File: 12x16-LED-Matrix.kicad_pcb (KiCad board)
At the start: 2 copper layers, 56 x 45 mm, 197 parts, among them J1 Conn_01x16, J2 Conn_01x12

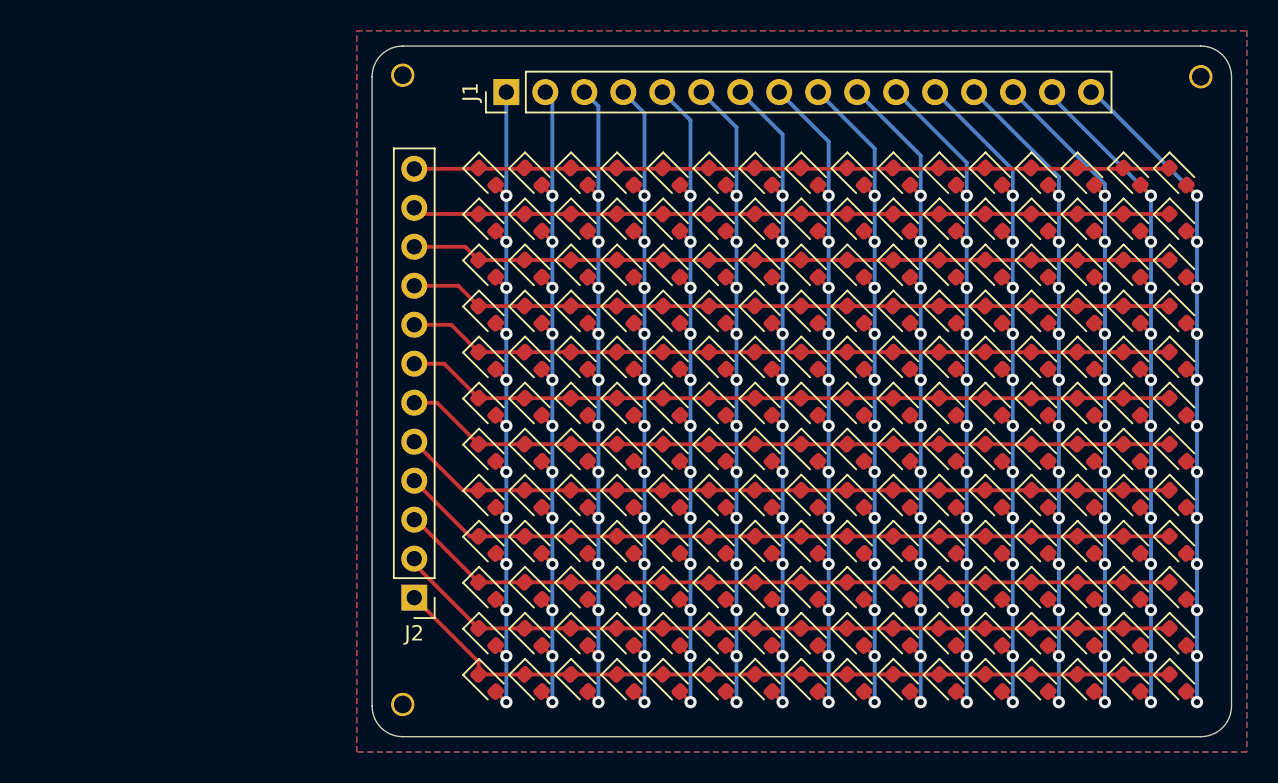
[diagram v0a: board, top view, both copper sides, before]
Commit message: Add silkscreen
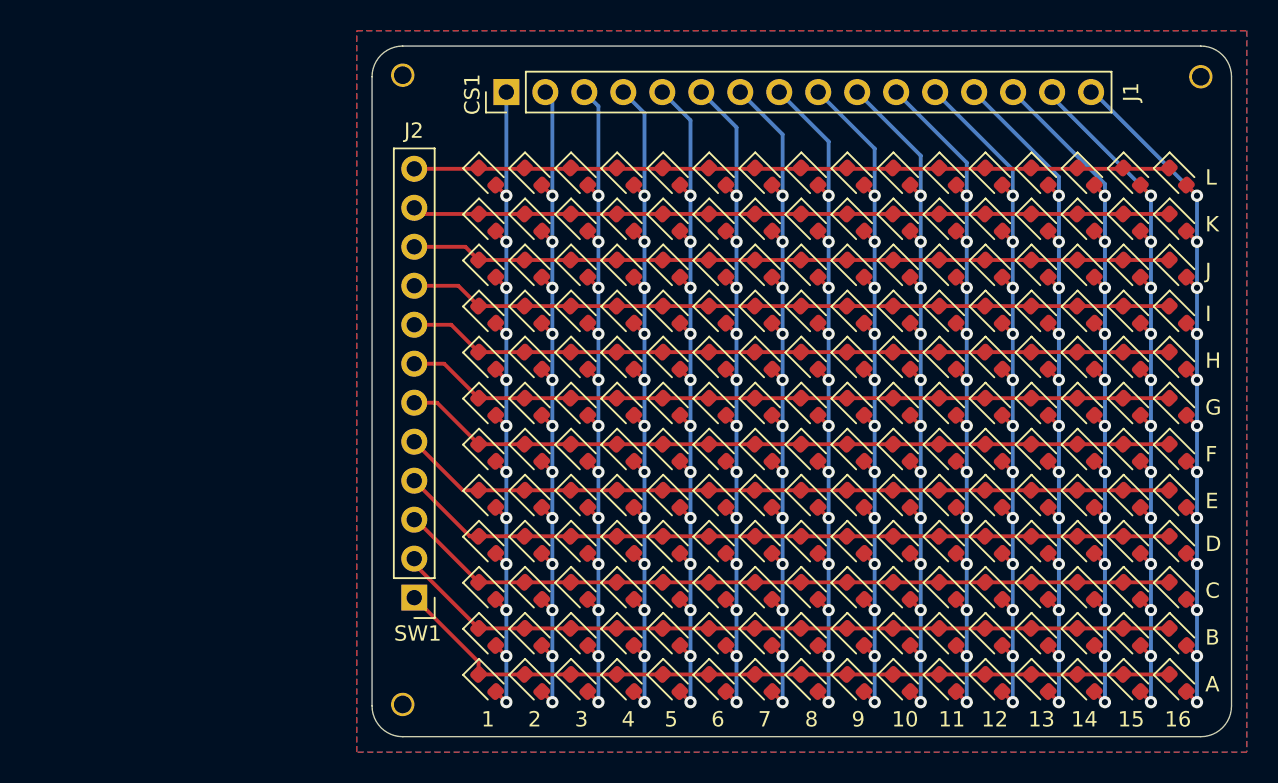
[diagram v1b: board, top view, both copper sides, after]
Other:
- board text added: "1"
- board text added: "10"
- board text added: "11"
- board text added: "12"
- board text added: "13"
- board text added: "14"
- board text added: "15"
- board text added: "16"
- board text added: "2"
- board text added: "3"
- board text added: "4"
- board text added: "5"
- board text added: "6"
- board text added: "7"
- board text added: "8"
- board text added: "9"
- board text added: "A"
- board text added: "B"
- board text added: "C"
- board text added: "CS1"
- board text added: "CS10"
- board text added: "CS11"
- board text added: "CS12"
- board text added: "CS13"
- board text added: "CS14"
- board text added: "CS15"
- board text added: "CS16"
- board text added: "CS2"
- board text added: "CS3"
- board text added: "CS4"
- board text added: "CS5"
- board text added: "CS6"
- board text added: "CS7"
- board text added: "CS8"
- board text added: "CS9"
- board text added: "D"
- board text added: "E"
- board text added: "F"
- board text added: "G"
- board text added: "H"
- board text added: "I"
- board text added: "J"
- board text added: "K"
- board text added: "L"
- board text added: "SW1"
- board text added: "SW10"
- board text added: "SW11"
- board text added: "SW12"
- board text added: "SW2"
- board text added: "SW3"
- board text added: "SW4"
- board text added: "SW5"
- board text added: "SW6"
- board text added: "SW7"
- board text added: "SW8"
- board text added: "SW9"

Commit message: Add ground pins, fix silkscreen
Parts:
- J1: value Conn_01x16 -> Conn_01x17; footprint Connector_PinHeader_2.54mm:PinHeader_1x16_P2.54mm_Vertical -> Connector_PinHeader_2.54mm:PinHeader_1x17_P2.54mm_Vertical
- J2: value Conn_01x12 -> Conn_01x13; footprint Connector_PinHeader_2.54mm:PinHeader_1x12_P2.54mm_Vertical -> Connector_PinHeader_2.54mm:PinHeader_1x13_P2.54mm_Vertical
- moved J1 0.50 mm to (83.8, 62.5)
- moved J2 0.26 mm to (78.0, 95.0)
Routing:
- added copper zone on B.Cu, net GND
- added copper zone on F.Cu, net GND
- removed copper zone on B.Cu, net (none)
- removed copper zone on F.Cu, net (none)
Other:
- board text added: "%%version%% %%date%%"
- board text added: "GND"
- board text added: "JLCJLCJLCJLC"
- board text removed: "16x12 LED matrix %%version%% %%date%%"

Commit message: Add driver directly to schematic
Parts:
- removed J2: Conn_01x13, Connector_PinHeader_2.54mm:PinHeader_1x13_P2.54mm_Vertical
- added C1: 0.47uF, Capacitor_SMD:C_0402_1005Metric, F.Cu at (57.9, 74.8)
- added C2: 0.47uF, Capacitor_SMD:C_0402_1005Metric, F.Cu at (60.8, 74.8)
- added C3: 0.47uF, Capacitor_SMD:C_0402_1005Metric, F.Cu at (57.9, 76.7)
- added C4: 0.1uF, Capacitor_SMD:C_0402_1005Metric, F.Cu at (57.9, 78.7)
- added C5: 0.1uF, Capacitor_SMD:C_0402_1005Metric, F.Cu at (69.1, 68.5)
- added C6: 0.1uF, Capacitor_SMD:C_0402_1005Metric, F.Cu at (60.8, 76.7)
- added C7: 0.47uF, Capacitor_SMD:C_0402_1005Metric, F.Cu at (72.0, 66.5)
- added R1: 100k, Resistor_SMD:R_0402_1005Metric, F.Cu at (66.2, 66.5)
- added R2: 100k, Resistor_SMD:R_0402_1005Metric, F.Cu at (69.1, 66.5)
- added R3: 100k, Resistor_SMD:R_0402_1005Metric, F.Cu at (66.2, 68.5)
- added R4: 20k, Resistor_SMD:R_0402_1005Metric, F.Cu at (66.2, 70.5)
- added U1: IS31FL3733B, Package_DFN_QFN:QFN-48-1EP_6x6mm_P0.4mm_EP4.3x4.3mm_ThermalVias, F.Cu at (60.6, 69.7)
- J1: value Conn_01x17 -> Conn_01x06; footprint Connector_PinHeader_2.54mm:PinHeader_1x17_P2.54mm_Vertical -> Connector_PinHeader_2.54mm:PinHeader_1x06_P2.54mm_Vertical
- moved J1 30.1 mm to (54.1, 67.9), turned to 0 degrees
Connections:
- net Net-(D1-Pad1) renamed SW1
- net Net-(D100-Pad1) renamed SW7
- net Net-(D113-Pad1) renamed SW8
- net Net-(D129-Pad1) renamed SW9
- net Net-(D145-Pad1) renamed SW10
- net Net-(D161-Pad1) renamed SW11
- net Net-(D17-Pad1) renamed SW2
- net Net-(D177-Pad1) renamed SW12
- net Net-(D33-Pad1) renamed SW3
- net Net-(D49-Pad1) renamed SW4
- net Net-(D65-Pad1) renamed SW5
- net Net-(D81-Pad1) renamed SW6
- D1 pad 2: Net-(D1-Pad2) -> CS1
- D10 pad 2: Net-(D10-Pad2) -> CS10
- D100 pad 2: Net-(D100-Pad2) -> CS4
- D101 pad 2: Net-(D101-Pad2) -> CS5
- D102 pad 2: Net-(D102-Pad2) -> CS6
- D103 pad 2: Net-(D103-Pad2) -> CS7
- D104 pad 2: Net-(D104-Pad2) -> CS8
- D105 pad 2: Net-(D105-Pad2) -> CS9
- D106 pad 2: Net-(D10-Pad2) -> CS10
- D107 pad 2: Net-(D107-Pad2) -> CS11
- D108 pad 2: Net-(D108-Pad2) -> CS12
- D109 pad 2: Net-(D109-Pad2) -> CS13
- D11 pad 2: Net-(D107-Pad2) -> CS11
- D110 pad 2: Net-(D110-Pad2) -> CS14
- D111 pad 2: Net-(D111-Pad2) -> CS15
- D112 pad 2: Net-(D112-Pad2) -> CS16
- D113 pad 2: Net-(D1-Pad2) -> CS1
- D114 pad 2: Net-(D114-Pad2) -> CS2
- D115 pad 2: Net-(D115-Pad2) -> CS3
- D116 pad 2: Net-(D100-Pad2) -> CS4
- D117 pad 2: Net-(D101-Pad2) -> CS5
- D118 pad 2: Net-(D102-Pad2) -> CS6
- D119 pad 2: Net-(D103-Pad2) -> CS7
- D12 pad 2: Net-(D108-Pad2) -> CS12
- D120 pad 2: Net-(D104-Pad2) -> CS8
- D121 pad 2: Net-(D105-Pad2) -> CS9
- D122 pad 2: Net-(D10-Pad2) -> CS10
- D123 pad 2: Net-(D107-Pad2) -> CS11
- D124 pad 2: Net-(D108-Pad2) -> CS12
- D125 pad 2: Net-(D109-Pad2) -> CS13
- D126 pad 2: Net-(D110-Pad2) -> CS14
- D127 pad 2: Net-(D111-Pad2) -> CS15
- D128 pad 2: Net-(D112-Pad2) -> CS16
- D129 pad 2: Net-(D1-Pad2) -> CS1
- D13 pad 2: Net-(D109-Pad2) -> CS13
- D130 pad 2: Net-(D114-Pad2) -> CS2
- D131 pad 2: Net-(D115-Pad2) -> CS3
- D132 pad 2: Net-(D100-Pad2) -> CS4
- D133 pad 2: Net-(D101-Pad2) -> CS5
- D134 pad 2: Net-(D102-Pad2) -> CS6
- D135 pad 2: Net-(D103-Pad2) -> CS7
- D136 pad 2: Net-(D104-Pad2) -> CS8
- D137 pad 2: Net-(D105-Pad2) -> CS9
- D138 pad 2: Net-(D10-Pad2) -> CS10
- D139 pad 2: Net-(D107-Pad2) -> CS11
- D14 pad 2: Net-(D110-Pad2) -> CS14
- D140 pad 2: Net-(D108-Pad2) -> CS12
- D141 pad 2: Net-(D109-Pad2) -> CS13
- D142 pad 2: Net-(D110-Pad2) -> CS14
- D143 pad 2: Net-(D111-Pad2) -> CS15
- D144 pad 2: Net-(D112-Pad2) -> CS16
- D145 pad 2: Net-(D1-Pad2) -> CS1
- D146 pad 2: Net-(D114-Pad2) -> CS2
- D147 pad 2: Net-(D115-Pad2) -> CS3
- D148 pad 2: Net-(D100-Pad2) -> CS4
- D149 pad 2: Net-(D101-Pad2) -> CS5
- D15 pad 2: Net-(D111-Pad2) -> CS15
- D150 pad 2: Net-(D102-Pad2) -> CS6
- D151 pad 2: Net-(D103-Pad2) -> CS7
- D152 pad 2: Net-(D104-Pad2) -> CS8
- D153 pad 2: Net-(D105-Pad2) -> CS9
- D154 pad 2: Net-(D10-Pad2) -> CS10
- D155 pad 2: Net-(D107-Pad2) -> CS11
- D156 pad 2: Net-(D108-Pad2) -> CS12
- D157 pad 2: Net-(D109-Pad2) -> CS13
- D158 pad 2: Net-(D110-Pad2) -> CS14
- D159 pad 2: Net-(D111-Pad2) -> CS15
- D16 pad 2: Net-(D112-Pad2) -> CS16
- D160 pad 2: Net-(D112-Pad2) -> CS16
- D161 pad 2: Net-(D1-Pad2) -> CS1
- D162 pad 2: Net-(D114-Pad2) -> CS2
- D163 pad 2: Net-(D115-Pad2) -> CS3
- D164 pad 2: Net-(D100-Pad2) -> CS4
- D165 pad 2: Net-(D101-Pad2) -> CS5
- D166 pad 2: Net-(D102-Pad2) -> CS6
- D167 pad 2: Net-(D103-Pad2) -> CS7
- D168 pad 2: Net-(D104-Pad2) -> CS8
- D169 pad 2: Net-(D105-Pad2) -> CS9
- D17 pad 2: Net-(D1-Pad2) -> CS1
- D170 pad 2: Net-(D10-Pad2) -> CS10
- D171 pad 2: Net-(D107-Pad2) -> CS11
- D172 pad 2: Net-(D108-Pad2) -> CS12
- D173 pad 2: Net-(D109-Pad2) -> CS13
- D174 pad 2: Net-(D110-Pad2) -> CS14
- D175 pad 2: Net-(D111-Pad2) -> CS15
- D176 pad 2: Net-(D112-Pad2) -> CS16
- D177 pad 2: Net-(D1-Pad2) -> CS1
- D178 pad 2: Net-(D114-Pad2) -> CS2
- D179 pad 2: Net-(D115-Pad2) -> CS3
- D18 pad 2: Net-(D114-Pad2) -> CS2
- D180 pad 2: Net-(D100-Pad2) -> CS4
- D181 pad 2: Net-(D101-Pad2) -> CS5
- D182 pad 2: Net-(D102-Pad2) -> CS6
- D183 pad 2: Net-(D103-Pad2) -> CS7
- D184 pad 2: Net-(D104-Pad2) -> CS8
- D185 pad 2: Net-(D105-Pad2) -> CS9
- D186 pad 2: Net-(D10-Pad2) -> CS10
- D187 pad 2: Net-(D107-Pad2) -> CS11
- D188 pad 2: Net-(D108-Pad2) -> CS12
- D189 pad 2: Net-(D109-Pad2) -> CS13
- D19 pad 2: Net-(D115-Pad2) -> CS3
- D190 pad 2: Net-(D110-Pad2) -> CS14
- D191 pad 2: Net-(D111-Pad2) -> CS15
- D192 pad 2: Net-(D112-Pad2) -> CS16
- D2 pad 2: Net-(D114-Pad2) -> CS2
- D20 pad 2: Net-(D100-Pad2) -> CS4
- D21 pad 2: Net-(D101-Pad2) -> CS5
- D22 pad 2: Net-(D102-Pad2) -> CS6
- D23 pad 2: Net-(D103-Pad2) -> CS7
- D24 pad 2: Net-(D104-Pad2) -> CS8
- D25 pad 2: Net-(D105-Pad2) -> CS9
- D26 pad 2: Net-(D10-Pad2) -> CS10
- D27 pad 2: Net-(D107-Pad2) -> CS11
- D28 pad 2: Net-(D108-Pad2) -> CS12
- D29 pad 2: Net-(D109-Pad2) -> CS13
- D3 pad 2: Net-(D115-Pad2) -> CS3
- D30 pad 2: Net-(D110-Pad2) -> CS14
- D31 pad 2: Net-(D111-Pad2) -> CS15
- D32 pad 2: Net-(D112-Pad2) -> CS16
- D33 pad 2: Net-(D1-Pad2) -> CS1
- D34 pad 2: Net-(D114-Pad2) -> CS2
- D35 pad 2: Net-(D115-Pad2) -> CS3
- D36 pad 2: Net-(D100-Pad2) -> CS4
- D37 pad 2: Net-(D101-Pad2) -> CS5
- D38 pad 2: Net-(D102-Pad2) -> CS6
- D39 pad 2: Net-(D103-Pad2) -> CS7
- D4 pad 2: Net-(D100-Pad2) -> CS4
- D40 pad 2: Net-(D104-Pad2) -> CS8
- D41 pad 2: Net-(D105-Pad2) -> CS9
- D42 pad 2: Net-(D10-Pad2) -> CS10
- D43 pad 2: Net-(D107-Pad2) -> CS11
- D44 pad 2: Net-(D108-Pad2) -> CS12
- D45 pad 2: Net-(D109-Pad2) -> CS13
- D46 pad 2: Net-(D110-Pad2) -> CS14
- D47 pad 2: Net-(D111-Pad2) -> CS15
- D48 pad 2: Net-(D112-Pad2) -> CS16
- D49 pad 2: Net-(D1-Pad2) -> CS1
- D5 pad 2: Net-(D101-Pad2) -> CS5
- D50 pad 2: Net-(D114-Pad2) -> CS2
- D51 pad 2: Net-(D115-Pad2) -> CS3
- D52 pad 2: Net-(D100-Pad2) -> CS4
- D53 pad 2: Net-(D101-Pad2) -> CS5
- D54 pad 2: Net-(D102-Pad2) -> CS6
- D55 pad 2: Net-(D103-Pad2) -> CS7
- D56 pad 2: Net-(D104-Pad2) -> CS8
- D57 pad 2: Net-(D105-Pad2) -> CS9
- D58 pad 2: Net-(D10-Pad2) -> CS10
- D59 pad 2: Net-(D107-Pad2) -> CS11
- D6 pad 2: Net-(D102-Pad2) -> CS6
- D60 pad 2: Net-(D108-Pad2) -> CS12
- D61 pad 2: Net-(D109-Pad2) -> CS13
- D62 pad 2: Net-(D110-Pad2) -> CS14
- D63 pad 2: Net-(D111-Pad2) -> CS15
- D64 pad 2: Net-(D112-Pad2) -> CS16
- D65 pad 2: Net-(D1-Pad2) -> CS1
- D66 pad 2: Net-(D114-Pad2) -> CS2
- D67 pad 2: Net-(D115-Pad2) -> CS3
- D68 pad 2: Net-(D100-Pad2) -> CS4
- D69 pad 2: Net-(D101-Pad2) -> CS5
- D7 pad 2: Net-(D103-Pad2) -> CS7
- D70 pad 2: Net-(D102-Pad2) -> CS6
- D71 pad 2: Net-(D103-Pad2) -> CS7
- D72 pad 2: Net-(D104-Pad2) -> CS8
- D73 pad 2: Net-(D105-Pad2) -> CS9
- D74 pad 2: Net-(D10-Pad2) -> CS10
- D75 pad 2: Net-(D107-Pad2) -> CS11
- D76 pad 2: Net-(D108-Pad2) -> CS12
- D77 pad 2: Net-(D109-Pad2) -> CS13
- D78 pad 2: Net-(D110-Pad2) -> CS14
- D79 pad 2: Net-(D111-Pad2) -> CS15
- D8 pad 2: Net-(D104-Pad2) -> CS8
- D80 pad 2: Net-(D112-Pad2) -> CS16
- D81 pad 2: Net-(D1-Pad2) -> CS1
- D82 pad 2: Net-(D114-Pad2) -> CS2
- D83 pad 2: Net-(D115-Pad2) -> CS3
- D84 pad 2: Net-(D100-Pad2) -> CS4
- D85 pad 2: Net-(D101-Pad2) -> CS5
- D86 pad 2: Net-(D102-Pad2) -> CS6
- D87 pad 2: Net-(D103-Pad2) -> CS7
- D88 pad 2: Net-(D104-Pad2) -> CS8
- D89 pad 2: Net-(D105-Pad2) -> CS9
- D9 pad 2: Net-(D105-Pad2) -> CS9
- D90 pad 2: Net-(D10-Pad2) -> CS10
- D91 pad 2: Net-(D107-Pad2) -> CS11
- D92 pad 2: Net-(D108-Pad2) -> CS12
- D93 pad 2: Net-(D109-Pad2) -> CS13
- D94 pad 2: Net-(D110-Pad2) -> CS14
- D95 pad 2: Net-(D111-Pad2) -> CS15
- D96 pad 2: Net-(D112-Pad2) -> CS16
- D97 pad 2: Net-(D1-Pad2) -> CS1
- D98 pad 2: Net-(D114-Pad2) -> CS2
- D99 pad 2: Net-(D115-Pad2) -> CS3
- J1 pad 1: Net-(D1-Pad2) -> +5V
- J1 pad 2: Net-(D114-Pad2) -> /SDA
- J1 pad 3: Net-(D115-Pad2) -> /SCL
- J1 pad 4: Net-(D100-Pad2) -> /SDB
- J1 pad 5: Net-(D101-Pad2) -> /INTB
- J1 pad 6: Net-(D102-Pad2) -> GND
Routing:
- net Net-(D112-Pad2): track 54.5 -> 0.00 mm, vias 12 -> 0
- net CS16: track 0.00 -> 54.5 mm, vias 0 -> 12
- net Net-(D111-Pad2): track 54.2 -> 0.00 mm, vias 12 -> 0
- net CS15: track 0.00 -> 54.2 mm, vias 0 -> 12
- net Net-(D110-Pad2): track 54.0 -> 0.00 mm, vias 12 -> 0
- net CS14: track 0.00 -> 54.0 mm, vias 0 -> 12
- net Net-(D109-Pad2): track 53.8 -> 0.00 mm, vias 12 -> 0
- net CS13: track 0.00 -> 53.8 mm, vias 0 -> 12
- net Net-(D108-Pad2): track 53.6 -> 0.00 mm, vias 12 -> 0
- net CS12: track 0.00 -> 53.6 mm, vias 0 -> 12
- net Net-(D107-Pad2): track 53.4 -> 0.00 mm, vias 12 -> 0
- net CS11: track 0.00 -> 53.4 mm, vias 0 -> 12
- net Net-(D10-Pad2): track 53.2 -> 0.00 mm, vias 12 -> 0
- net CS10: track 0.00 -> 53.2 mm, vias 0 -> 12
- net Net-(D105-Pad2): track 53.0 -> 0.00 mm, vias 12 -> 0
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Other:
- board text removed: "A"
- board text removed: "B"
- board text removed: "C"
- board text removed: "CS10"
- board text removed: "CS11"
- board text removed: "CS12"
- board text removed: "CS13"
- board text removed: "CS14"
- board text removed: "CS15"
- board text removed: "CS16"
- board text removed: "CS2"
- board text removed: "CS3"
- board text removed: "CS4"
- board text removed: "CS5"
- board text removed: "CS6"
- board text removed: "CS7"
- board text removed: "CS8"
- board text removed: "CS9"
- board text removed: "D"
- board text removed: "E"
- board text removed: "F"
- board text removed: "G"
- board text removed: "GND"
- board text removed: "H"
- board text removed: "I"
- board text removed: "J"
- board text removed: "K"
- board text removed: "L"
- board text removed: "SW10"
- board text removed: "SW11"
- board text removed: "SW12"
- board text removed: "SW2"
- board text removed: "SW3"
- board text removed: "SW4"
- board text removed: "SW5"
- board text removed: "SW6"
- board text removed: "SW7"
- board text removed: "SW8"
- board text removed: "SW9"
